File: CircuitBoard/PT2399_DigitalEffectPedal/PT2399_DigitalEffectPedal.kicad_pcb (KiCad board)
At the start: 4 copper layers, 75 x 78 mm, 130 parts, among them J12 AudioOutput_connector, J15 Encoder_connector, J17 Encoder_board_connector, J8 AudioInput_connector, J9 GND_POWER_INDICATOR, Q1 BC547, Q2 BC547, U1 PT2399, U2 MCP6002-xSN, U3 MCP6002-xSN, U4 4066, U5 PT2399, U6 LM317_SOT-223, U7 AMS1117-5.0, U8 PIC16F72, Y1 Crystal

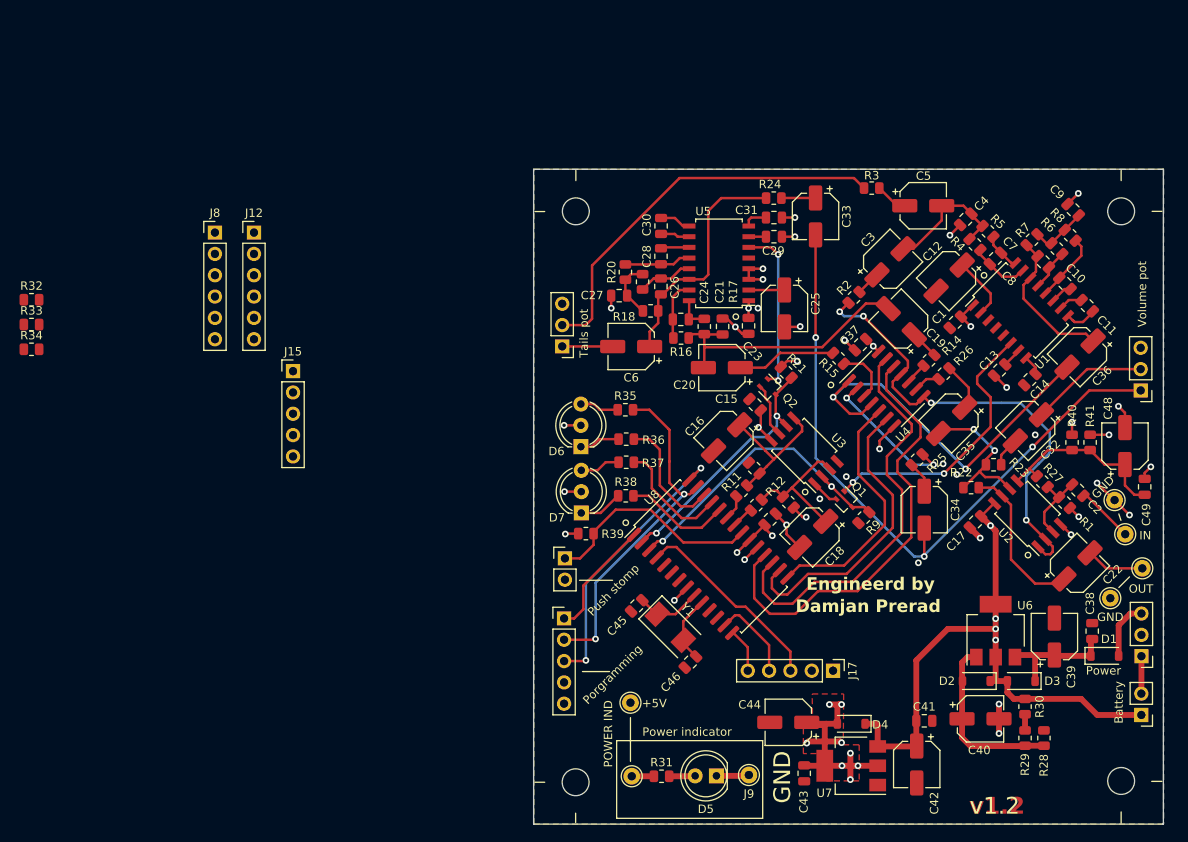
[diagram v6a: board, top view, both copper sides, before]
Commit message: Added GND vias to connect power planes
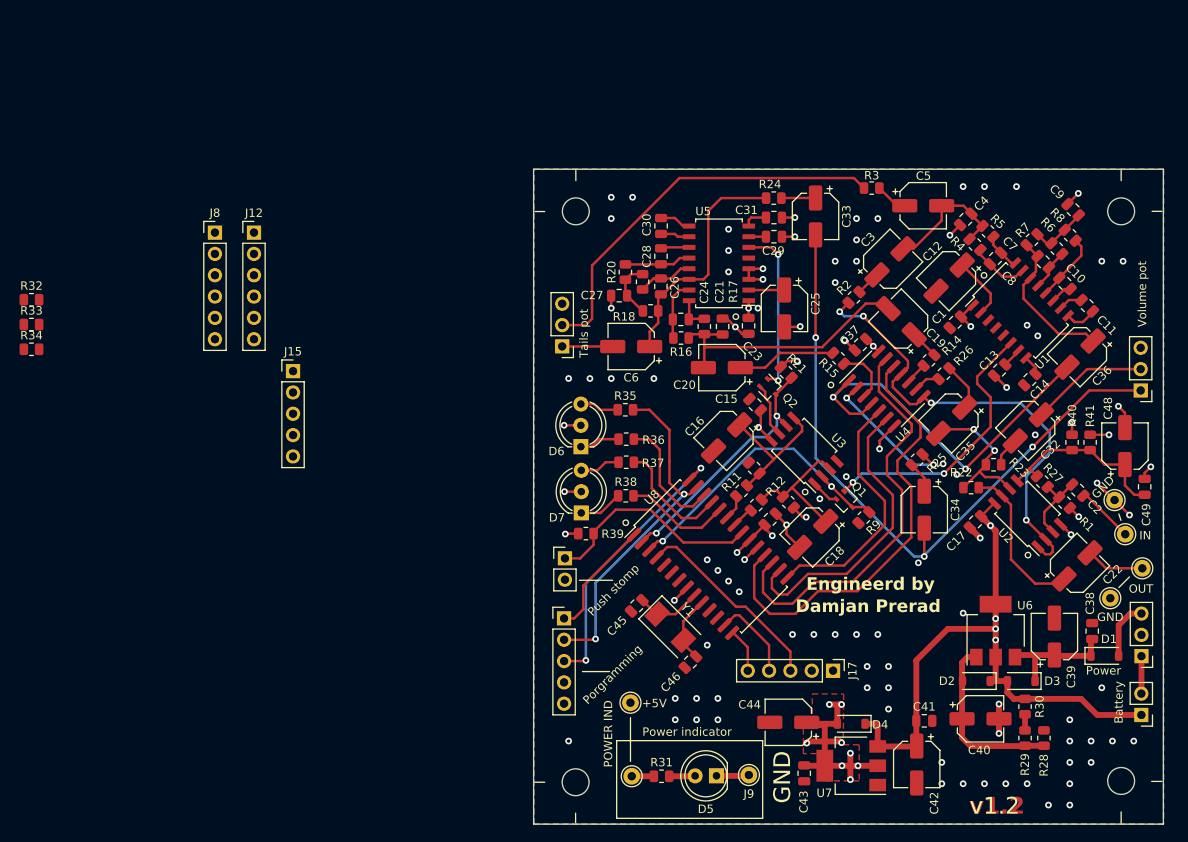
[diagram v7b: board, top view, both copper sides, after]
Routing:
- net GNDA: vias 34 -> 97
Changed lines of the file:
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@@
   (segment (start 151.925 92.6922) (end 153.162 93.9292) (width 0.7) (layer "F.Cu") (net 2))
   (via (at 126.6952 66.548) (size 0.8) (drill 0.4) (layers "F.Cu" "B.Cu") (free) (net 2))
+  (via (at 156.21 123.19) (size 0.8) (drill 0.4) (layers "F.Cu" "B.Cu") (free) (net 2))
+  (via (at 153.67 52.07) (size 0.8) (drill 0.4) (layers "F.Cu" "B.Cu") (free) (net 2))
+  (via (at 123.19 62.23) (size 0.8) (drill 0.4) (layers "F.Cu" "B.Cu") (free) (net 2))
   (via (at 173.482 85.4456) (size 0.8) (drill 0.4) (layers "F.Cu" "B.Cu") (net 2))
+  (via (at 133.35 105.41) (size 0.8) (drill 0.4) (layers "F.Cu" "B.Cu") (free) (net 2))
+  (via (at 161.29 125.73) (size 0.8) (drill 0.4) (layers "F.Cu" "B.Cu") (free) (net 2))
   (via (at 127.285999 61.851) (size 0.8) (drill 0.4) (layers "F.Cu" "B.Cu") (net 2))
+  (via (at 104.14 74.93) (size 0.8) (drill 0.4) (layers "F.Cu" "B.Cu") (free) (net 2))
   (via (at 131.3688 72.8472) (size 0.8) (drill 0.4) (layers "F.Cu" "B.Cu") (net 2))
+  (via (at 130.81 105.41) (size 0.8) (drill 0.4) (layers "F.Cu" "B.Cu") (free) (net 2))
   (via (at 132.4356 91.44) (size 0.8) (drill 0.4) (layers "F.Cu" "B.Cu") (free) (net 2))
+  (via (at 142.24 109.22) (size 0.8) (drill 0.4) (layers "F.Cu" "B.Cu") (free) (net 2))
+  (via (at 163.83 123.19) (size 0.8) (drill 0.4) (layers "F.Cu" "B.Cu") (free) (net 2))
   (via (at 167.0812 87.376) (size 0.8) (drill 0.4) (layers "F.Cu" "B.Cu") (net 2))
+  (via (at 109.22 55.88) (size 0.8) (drill 0.4) (layers "F.Cu" "B.Cu") (free) (net 2))
+  (via (at 140.97 55.88) (size 0.8) (drill 0.4) (layers "F.Cu" "B.Cu") (free) (net 2))
+  (via (at 170.18 60.96) (size 0.8) (drill 0.4) (layers "F.Cu" "B.Cu") (free) (net 2))
+  (via (at 158.75 123.19) (size 0.8) (drill 0.4) (layers "F.Cu" "B.Cu") (free) (net 2))
   (via (at 145.796 96.8756) (size 0.8) (drill 0.4) (layers "F.Cu" "B.Cu") (free) (net 2))
+  (via (at 160.02 69.85) (size 0.8) (drill 0.4) (layers "F.Cu" "B.Cu") (free) (net 2))
+  (via (at 138.43 55.88) (size 0.8) (drill 0.4) (layers "F.Cu" "B.Cu") (free) (net 2))
+  (via (at 123.19 57.15) (size 0.8) (drill 0.4) (layers "F.Cu" "B.Cu") (free) (net 2))
   (via (at 155.4 117.2) (size 0.8) (drill 0.4) (layers "F.Cu" "B.Cu") (net 2))
+  (via (at 116.84 113.03) (size 0.8) (drill 0.4) (layers "F.Cu" "B.Cu") (free) (net 2))
   (via (at 116.7384 101.346) (size 0.8) (drill 0.4) (layers "F.Cu" "B.Cu") (net 2))
+  (via (at 163.83 118.11) (size 0.8) (drill 0.4) (layers "F.Cu" "B.Cu") (free) (net 2))
+  (via (at 109.22 53.34) (size 0.8) (drill 0.4) (layers "F.Cu" "B.Cu") (free) (net 2))
   (via (at 170.942 91.186) (size 0.8) (drill 0.4) (layers "F.Cu" "B.Cu") (net 2))
+  (via (at 138.43 60.96) (size 0.8) (drill 0.4) (layers "F.Cu" "B.Cu") (free) (net 2))
   (via (at 131.096 58.041) (size 0.8) (drill 0.4) (layers "F.Cu" "B.Cu") (net 2))
+  (via (at 119.38 113.03) (size 0.8) (drill 0.4) (layers "F.Cu" "B.Cu") (free) (net 2))
   (via (at 125.1 96.5) (size 0.8) (drill 0.4) (layers "F.Cu" "B.Cu") (net 2))
+  (via (at 111.76 53.34) (size 0.8) (drill 0.4) (layers "F.Cu" "B.Cu") (free) (net 2))
+  (via (at 166.37 118.11) (size 0.8) (drill 0.4) (layers "F.Cu" "B.Cu") (free) (net 2))
+  (via (at 121.92 113.03) (size 0.8) (drill 0.4) (layers "F.Cu" "B.Cu") (free) (net 2))
   (via (at 163.9824 93.5228) (size 0.8) (drill 0.4) (layers "F.Cu" "B.Cu") (net 2))
   (via (at 153.162 93.9292) (size 0.8) (drill 0.4) (layers "F.Cu" "B.Cu") (net 2))
   (via (at 124.0028 68.7832) (size 0.8) (drill 0.4) (layers "F.Cu" "B.Cu") (net 2))
   (via (at 137.2108 86.614) (size 0.8) (drill 0.4) (layers "F.Cu" "B.Cu") (free) (net 2))
+  (via (at 158.75 68.58) (size 0.8) (drill 0.4) (layers "F.Cu" "B.Cu") (free) (net 2))
   (via (at 109.22 66.548) (size 0.8) (drill 0.4) (layers "F.Cu" "B.Cu") (net 2))
+  (via (at 119.38 115.57) (size 0.8) (drill 0.4) (layers "F.Cu" "B.Cu") (free) (net 2))
+  (via (at 139.7 109.22) (size 0.8) (drill 0.4) (layers "F.Cu" "B.Cu") (free) (net 2))
+  (via (at 167.64 111.76) (size 0.8) (drill 0.4) (layers "F.Cu" "B.Cu") (free) (net 2))
+  (via (at 138.43 105.41) (size 0.8) (drill 0.4) (layers "F.Cu" "B.Cu") (free) (net 2))
   (via (at 137.0076 70.358) (size 0.8) (drill 0.4) (layers "F.Cu" "B.Cu") (net 2))
+  (via (at 171.45 118.11) (size 0.8) (drill 0.4) (layers "F.Cu" "B.Cu") (free) (net 2))
   (via (at 131.096 55.755) (size 0.8) (drill 0.4) (layers "F.Cu" "B.Cu") (net 2))
+  (via (at 167.64 60.96) (size 0.8) (drill 0.4) (layers "F.Cu" "B.Cu") (free) (net 2))
+  (via (at 121.92 115.57) (size 0.8) (drill 0.4) (layers "F.Cu" "B.Cu") (free) (net 2))
+  (via (at 153.67 123.19) (size 0.8) (drill 0.4) (layers "F.Cu" "B.Cu") (free) (net 2))
   (via (at 149.5552 57.8612) (size 0.8) (drill 0.4) (layers "F.Cu" "B.Cu") (net 2))
   (via (at 134.0612 89.2556) (size 0.8) (drill 0.4) (layers "F.Cu" "B.Cu") (free) (net 2))
+  (via (at 148.59 123.19) (size 0.8) (drill 0.4) (layers "F.Cu" "B.Cu") (free) (net 2))
+  (via (at 151.13 123.19) (size 0.8) (drill 0.4) (layers "F.Cu" "B.Cu") (free) (net 2))
+  (via (at 120.65 96.52) (size 0.8) (drill 0.4) (layers "F.Cu" "B.Cu") (free) (net 2))
+  (via (at 121.92 97.79) (size 0.8) (drill 0.4) (layers "F.Cu" "B.Cu") (free) (net 2))
+  (via (at 114.3 74.93) (size 0.8) (drill 0.4) (layers "F.Cu" "B.Cu") (free) (net 2))
+  (via (at 168.91 118.11) (size 0.8) (drill 0.4) (layers "F.Cu" "B.Cu") (free) (net 2))
   (via (at 130.0988 92.3544) (size 0.8) (drill 0.4) (layers "F.Cu" "B.Cu") (net 2))
+  (via (at 124.46 100.33) (size 0.8) (drill 0.4) (layers "F.Cu" "B.Cu") (free) (net 2))
   (via (at 141.1732 83.312) (size 0.8) (drill 0.4) (layers "F.Cu" "B.Cu") (free) (net 2))
+  (via (at 138.43 58.42) (size 0.8) (drill 0.4) (layers "F.Cu" "B.Cu") (free) (net 2))
+  (via (at 106.68 74.93) (size 0.8) (drill 0.4) (layers "F.Cu" "B.Cu") (free) (net 2))
   (via (at 148.7424 85.09) (size 0.8) (drill 0.4) (layers "F.Cu" "B.Cu") (free) (net 2))
+  (via (at 139.7 111.76) (size 0.8) (drill 0.4) (layers "F.Cu" "B.Cu") (free) (net 2))
   (via (at 159.7152 81.6356) (size 0.8) (drill 0.4) (layers "F.Cu" "B.Cu") (free) (net 2))
   (via (at 164.8968 91.3892) (size 0.8) (drill 0.4) (layers "F.Cu" "B.Cu") (net 2))
+  (via (at 148.59 120.65) (size 0.8) (drill 0.4) (layers "F.Cu" "B.Cu") (free) (net 2))
+  (via (at 163.83 115.57) (size 0.8) (drill 0.4) (layers "F.Cu" "B.Cu") (free) (net 2))
   (via (at 150.368 86.36) (size 0.8) (drill 0.4) (layers "F.Cu" "B.Cu") (free) (net 2))
+  (via (at 166.37 120.65) (size 0.8) (drill 0.4) (layers "F.Cu" "B.Cu") (free) (net 2))
   (via (at 131.7244 68.7324) (size 0.8) (drill 0.4) (layers "F.Cu" "B.Cu") (net 2))
   (via (at 164.846 52.8828) (size 0.8) (drill 0.4) (layers "F.Cu" "B.Cu") (net 2))
+  (via (at 135.89 60.96) (size 0.8) (drill 0.4) (layers "F.Cu" "B.Cu") (free) (net 2))
+  (via (at 157.48 52.07) (size 0.8) (drill 0.4) (layers "F.Cu" "B.Cu") (free) (net 2))
+  (via (at 142.24 114.3) (size 0.8) (drill 0.4) (layers "F.Cu" "B.Cu") (free) (net 2))
+  (via (at 142.24 111.76) (size 0.8) (drill 0.4) (layers "F.Cu" "B.Cu") (free) (net 2))
   (via (at 169.6212 78.232) (size 0.8) (drill 0.4) (layers "F.Cu" "B.Cu") (net 2))
+  (via (at 140.97 105.41) (size 0.8) (drill 0.4) (layers "F.Cu" "B.Cu") (free) (net 2))
   (via (at 168.5036 81.6356) (size 0.8) (drill 0.4) (layers "F.Cu" "B.Cu") (net 2))
+  (via (at 104.14 118.11) (size 0.8) (drill 0.4) (layers "F.Cu" "B.Cu") (free) (net 2))
+  (via (at 109.22 74.93) (size 0.8) (drill 0.4) (layers "F.Cu" "B.Cu") (free) (net 2))
+  (via (at 163.83 120.65) (size 0.8) (drill 0.4) (layers "F.Cu" "B.Cu") (free) (net 2))
   (via (at 155.4 113.7) (size 0.8) (drill 0.4) (layers "F.Cu" "B.Cu") (net 2))
+  (via (at 135.89 63.5) (size 0.8) (drill 0.4) (layers "F.Cu" "B.Cu") (free) (net 2))
   (via (at 156.3116 75.9968) (size 0.8) (drill 0.4) (layers "F.Cu" "B.Cu") (net 2))
+  (via (at 135.89 105.41) (size 0.8) (drill 0.4) (layers "F.Cu" "B.Cu") (free) (net 2))
+  (via (at 116.84 115.57) (size 0.8) (drill 0.4) (layers "F.Cu" "B.Cu") (free) (net 2))
+  (via (at 123.19 99.06) (size 0.8) (drill 0.4) (layers "F.Cu" "B.Cu") (free) (net 2))
+  (via (at 151.13 102.87) (size 0.8) (drill 0.4) (layers "F.Cu" "B.Cu") (free) (net 2))
+  (via (at 163.83 125.73) (size 0.8) (drill 0.4) (layers "F.Cu" "B.Cu") (free) (net 2))
+  (via (at 120.65 106.68) (size 0.8) (drill 0.4) (layers "F.Cu" "B.Cu") (free) (net 2))
   (via (at 127.286 63.121) (size 0.8) (drill 0.4) (layers "F.Cu" "B.Cu") (net 2))
+  (via (at 151.13 52.07) (size 0.8) (drill 0.4) (layers "F.Cu" "B.Cu") (free) (net 2))
+  (via (at 123.19 59.69) (size 0.8) (drill 0.4) (layers "F.Cu" "B.Cu") (free) (net 2))
   (segment (start 164.065811 87.553249) (end 162.55953 89.05953) (width 0.3) (layer "F.Cu") (net 3))
   (segment (start 162.55953 89.05953) (end 162.40953 89.05953) (width 0.3) (layer "F.Cu") (net 3))
